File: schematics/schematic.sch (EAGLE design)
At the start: 47 parts, among them IC1 74HC365, T1 BC547, X5 PN61729-S

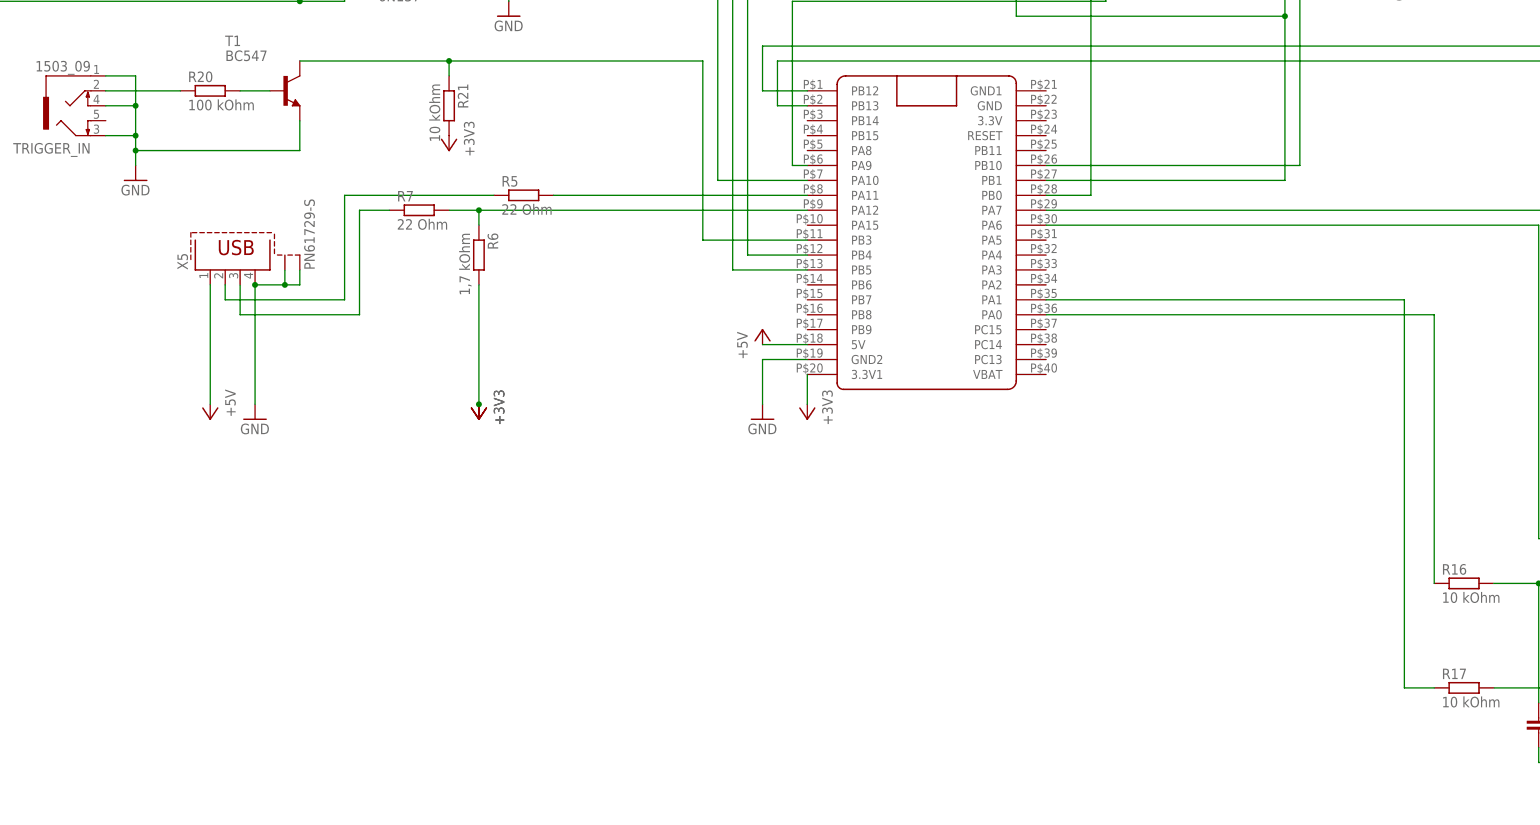
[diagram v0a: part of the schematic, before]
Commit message: added eeprom chip to schematic
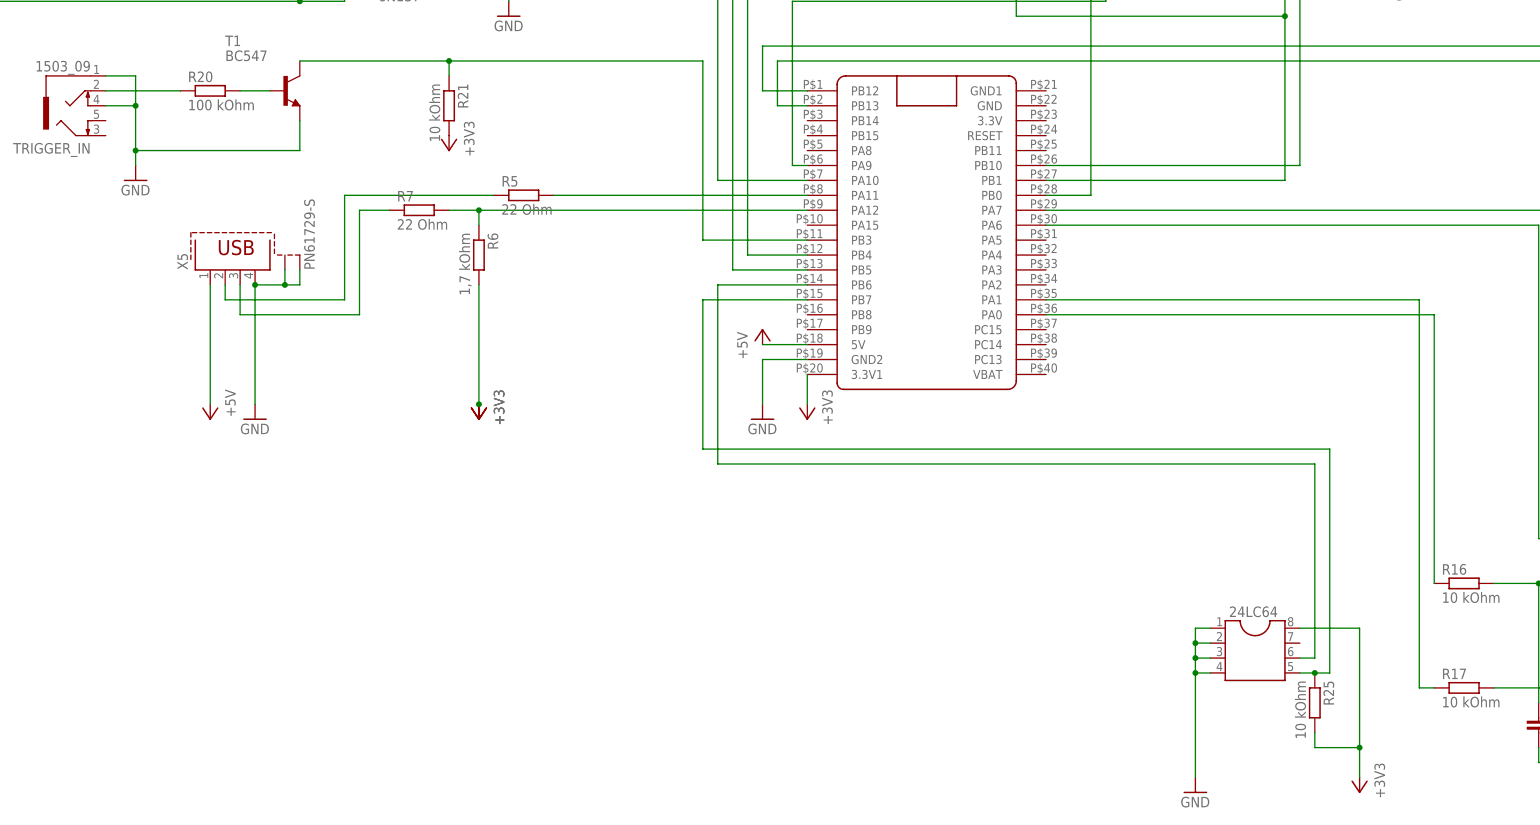
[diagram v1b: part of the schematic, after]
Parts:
- added 24LC64: (no value), ic-package:DIL8
- added R25: 10 kOhm, rcl:R-EU_0207/10
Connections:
- new net PB6: 24LC64.6, U$1.PB6
- new net PB7: 24LC64.5, R25.1, U$1.PB7
- net +3V3: now also 24LC64.8, R25.2
- net GND: now also 24LC64.1, 24LC64.2, 24LC64.3, 24LC64.4; no longer TRIGGER_IN.3
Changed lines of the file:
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@@
 <part name="GND10" library="supply1" library_urn="urn:adsk.eagle:library:371" deviceset="GND" device=""/>
 <part name="R23" library="rcl" library_urn="urn:adsk.eagle:library:334" deviceset="R-EU_" device="0207/10" package3d_urn="urn:adsk.eagle:package:23491/2" value="1 kOhm"/>
+<part name="24LC64" library="ic-package" library_urn="urn:adsk.eagle:library:239" deviceset="DIL8" device="" package3d_urn="urn:adsk.eagle:package:29519/2"/>
+<part name="GND11" library="supply1" library_urn="urn:adsk.eagle:library:371" deviceset="GND" device=""/>
+<part name="+3V5" library="supply1" library_urn="urn:adsk.eagle:library:371" deviceset="+3V3" device=""/>
+<part name="R25" library="rcl" library_urn="urn:adsk.eagle:library:334" deviceset="R-EU_" device="0207/10" package3d_urn="urn:adsk.eagle:package:23491/2" value="10 kOhm"/>
 </parts>
 <sheets>
@@
 <attribute name="NAME" x="148.8186" y="138.43" size="1.778" layer="95" rot="R270"/>
 <attribute name="VALUE" x="144.018" y="138.43" size="1.778" layer="96" rot="R270"/>
+</instance>
+<instance part="24LC64" gate="G$1" x="119.38" y="-25.4" smashed="yes">
+<attribute name="NAME" x="114.935" y="-20.955" size="1.778" layer="95"/>
+<attribute name="VALUE" x="114.935" y="-34.29" size="1.778" layer="96"/>
+</instance>
+<instance part="GND11" gate="1" x="109.22" y="-50.8" smashed="yes">
+<attribute name="VALUE" x="106.68" y="-53.34" size="1.778" layer="96"/>
+</instance>
+<instance part="+3V5" gate="G$1" x="137.16" y="-50.8" smashed="yes" rot="R180">
+<attribute name="VALUE" x="139.7" y="-45.72" size="1.778" layer="96" rot="R270"/>
+</instance>
+<instance part="R25" gate="G$1" x="129.54" y="-35.56" smashed="yes" rot="R270">
+<attribute name="NAME" x="131.0386" y="-31.75" size="1.778" layer="95" rot="R270"/>
+<attribute name="VALUE" x="126.238" y="-31.75" size="1.778" layer="96" rot="R270"/>
 </instance>
 </instances>
@@
 <wire x1="-71.12" y1="71.12" x2="-71.12" y2="66.04" width="0.1524" layer="91"/>
 <pinref part="TRIGGER_IN" gate="G$1" pin="4"/>
-<wire x1="-71.12" y1="66.04" x2="-71.12" y2="60.96" width="0.1524" layer="91"/>
-<wire x1="-71.12" y1="60.96" x2="-71.12" y2="58.42" width="0.1524" layer="91"/>
+<wire x1="-71.12" y1="66.04" x2="-71.12" y2="58.42" width="0.1524" layer="91"/>
 <wire x1="-71.12" y1="58.42" x2="-71.12" y2="55.88" width="0.1524" layer="91"/>
 <wire x1="-76.2" y1="66.04" x2="-71.12" y2="66.04" width="0.1524" layer="91"/>
 <junction x="-71.12" y="66.04"/>
-<pinref part="TRIGGER_IN" gate="G$1" pin="3"/>
-<wire x1="-76.2" y1="60.96" x2="-71.12" y2="60.96" width="0.1524" layer="91"/>
-<junction x="-71.12" y="60.96"/>
 <wire x1="-43.18" y1="58.42" x2="-71.12" y2="58.42" width="0.1524" layer="91"/>
 <junction x="-71.12" y="58.42"/>
@@
 <junction x="139.7" y="147.32"/>
 </segment>
+<segment>
+<pinref part="24LC64" gate="G$1" pin="4"/>
+<pinref part="GND11" gate="1" pin="GND"/>
+<wire x1="111.76" y1="-30.48" x2="109.22" y2="-30.48" width="0.1524" layer="91"/>
+<wire x1="109.22" y1="-30.48" x2="109.22" y2="-48.26" width="0.1524" layer="91"/>
+<pinref part="24LC64" gate="G$1" pin="3"/>
+<wire x1="111.76" y1="-27.94" x2="109.22" y2="-27.94" width="0.1524" layer="91"/>
+<wire x1="109.22" y1="-27.94" x2="109.22" y2="-30.48" width="0.1524" layer="91"/>
+<junction x="109.22" y="-30.48"/>
+<pinref part="24LC64" gate="G$1" pin="2"/>
+<wire x1="111.76" y1="-25.4" x2="109.22" y2="-25.4" width="0.1524" layer="91"/>
+<wire x1="109.22" y1="-25.4" x2="109.22" y2="-27.94" width="0.1524" layer="91"/>
+<junction x="109.22" y="-27.94"/>
+<pinref part="24LC64" gate="G$1" pin="1"/>
+<wire x1="111.76" y1="-22.86" x2="109.22" y2="-22.86" width="0.1524" layer="91"/>
+<wire x1="109.22" y1="-22.86" x2="109.22" y2="-25.4" width="0.1524" layer="91"/>
+<junction x="109.22" y="-25.4"/>
+</segment>
 </net>
 <net name="PB12" class="0">
@@
 <pinref part="+3V4" gate="G$1" pin="+3V3"/>
 </segment>
+<segment>
+<pinref part="24LC64" gate="G$1" pin="8"/>
+<pinref part="+3V5" gate="G$1" pin="+3V3"/>
+<wire x1="127" y1="-22.86" x2="137.16" y2="-22.86" width="0.1524" layer="91"/>
+<wire x1="137.16" y1="-22.86" x2="137.16" y2="-43.18" width="0.1524" layer="91"/>
+<pinref part="R25" gate="G$1" pin="2"/>
+<wire x1="137.16" y1="-43.18" x2="137.16" y2="-48.26" width="0.1524" layer="91"/>
+<wire x1="129.54" y1="-40.64" x2="129.54" y2="-43.18" width="0.1524" layer="91"/>
+<wire x1="129.54" y1="-43.18" x2="137.16" y2="-43.18" width="0.1524" layer="91"/>
+<junction x="137.16" y="-43.18"/>
+</segment>
 </net>
 <net name="PA2" class="0">
@@
 <segment>
 <pinref part="R17" gate="G$1" pin="1"/>
-<wire x1="149.86" y1="-33.02" x2="144.78" y2="-33.02" width="0.1524" layer="91"/>
+<wire x1="149.86" y1="-33.02" x2="147.32" y2="-33.02" width="0.1524" layer="91"/>
 <pinref part="U$1" gate="G$1" pin="PA1"/>
-<wire x1="144.78" y1="-33.02" x2="144.78" y2="33.02" width="0.1524" layer="91"/>
-<wire x1="144.78" y1="33.02" x2="83.82" y2="33.02" width="0.1524" layer="91"/>
+<wire x1="147.32" y1="-33.02" x2="147.32" y2="33.02" width="0.1524" layer="91"/>
+<wire x1="147.32" y1="33.02" x2="83.82" y2="33.02" width="0.1524" layer="91"/>
 </segment>
 </net>
@@
 </segment>
 </net>
+<net name="PB6" class="0">
+<segment>
+<pinref part="U$1" gate="G$1" pin="PB6"/>
+<wire x1="43.18" y1="35.56" x2="27.94" y2="35.56" width="0.1524" layer="91"/>
+<wire x1="27.94" y1="35.56" x2="27.94" y2="5.08" width="0.1524" layer="91"/>
+<wire x1="27.94" y1="5.08" x2="129.54" y2="5.08" width="0.1524" layer="91"/>
+<pinref part="24LC64" gate="G$1" pin="6"/>
+<wire x1="129.54" y1="5.08" x2="129.54" y2="-27.94" width="0.1524" layer="91"/>
+<wire x1="129.54" y1="-27.94" x2="127" y2="-27.94" width="0.1524" layer="91"/>
+</segment>
+</net>
+<net name="PB7" class="0">
+<segment>
+<pinref part="24LC64" gate="G$1" pin="5"/>
+<wire x1="127" y1="-30.48" x2="129.54" y2="-30.48" width="0.1524" layer="91"/>
+<wire x1="129.54" y1="-30.48" x2="132.08" y2="-30.48" width="0.1524" layer="91"/>
+<wire x1="132.08" y1="-30.48" x2="132.08" y2="7.62" width="0.1524" layer="91"/>
+<wire x1="132.08" y1="7.62" x2="25.4" y2="7.62" width="0.1524" layer="91"/>
+<wire x1="25.4" y1="7.62" x2="25.4" y2="33.02" width="0.1524" layer="91"/>
+<pinref part="U$1" gate="G$1" pin="PB7"/>
+<wire x1="25.4" y1="33.02" x2="43.18" y2="33.02" width="0.1524" layer="91"/>
+<pinref part="R25" gate="G$1" pin="1"/>
+<junction x="129.54" y="-30.48"/>
+</segment>
+</net>

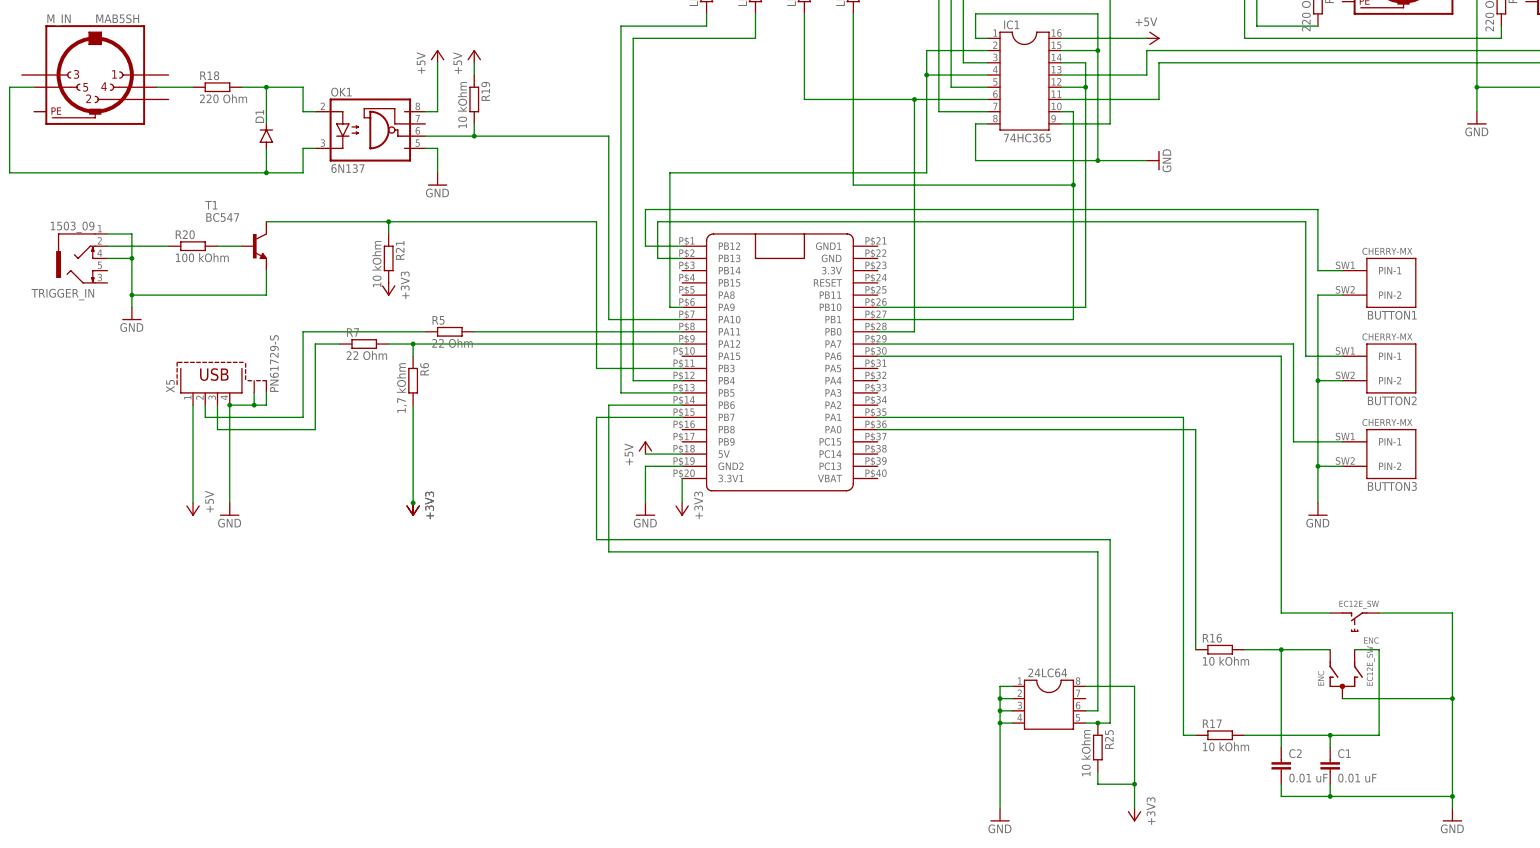
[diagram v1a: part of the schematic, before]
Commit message: added lcd8x2 display
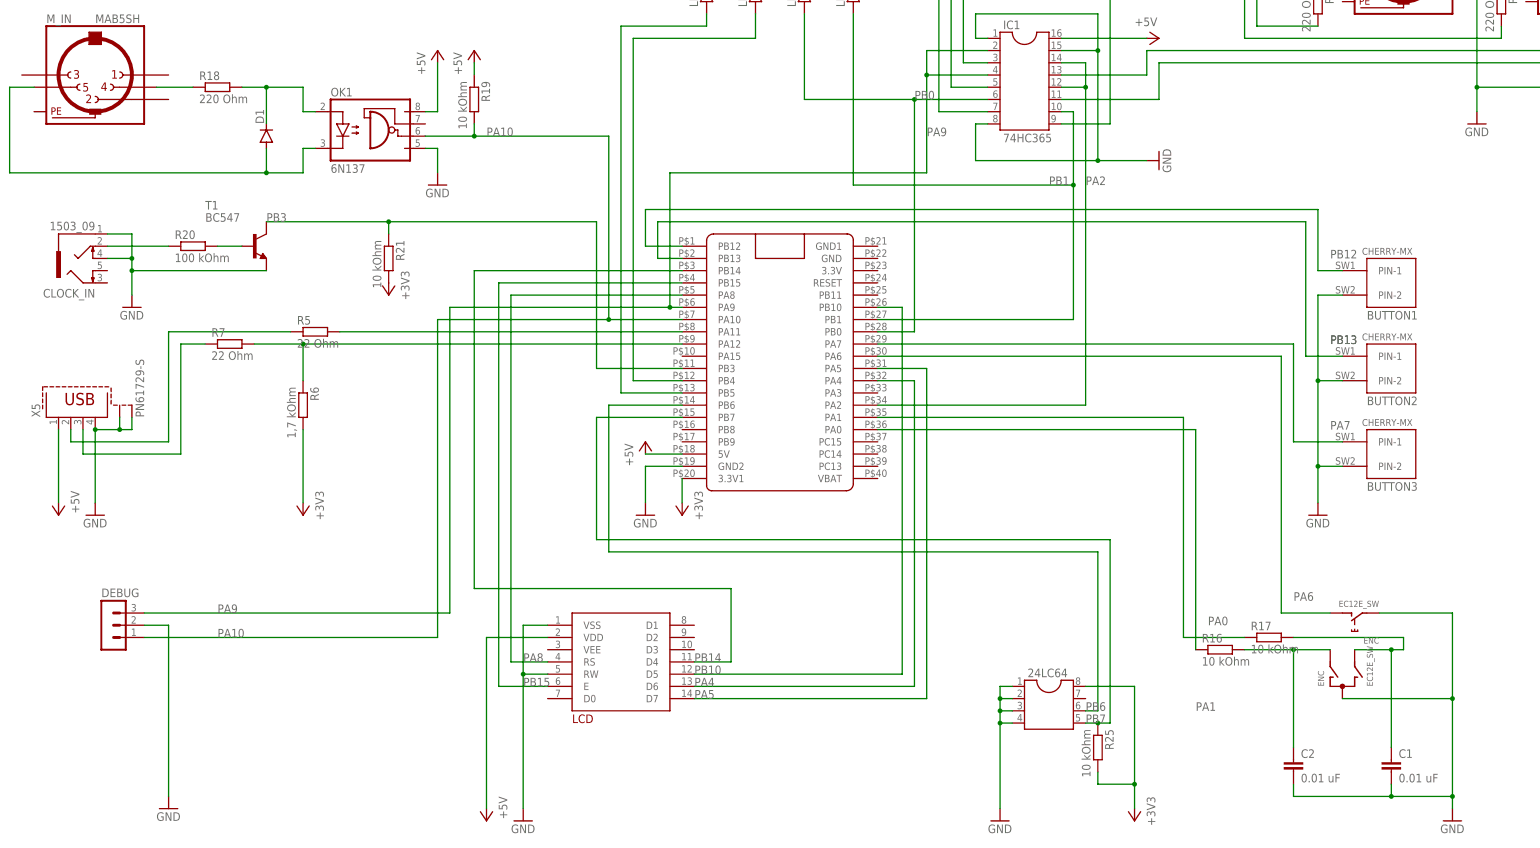
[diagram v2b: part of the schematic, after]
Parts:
- added DEBUG: (no value), con-lstb:MA03-1
- added LCD: LCD-MODUL2X8, lcd082dip:LCD-MODUL2X8
- renumbered TRIGGER_IN to CLOCK_IN
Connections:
- net N$22 renamed PA6
- net N$27 renamed PB3
- new net PA4: LCD.D6, U$1.PA4
- new net PA5: LCD.D7, U$1.PA5
- new net PA8: LCD.RS, U$1.PA8
- new net PA9: DEBUG.3, IC1.2, IC1.4, U$1.PA9
- new net PB14: LCD.D4, U$1.PB14
- new net PB15: LCD.E, U$1.PB15
- net +5V: now also LCD.VDD
- net GND: now also DEBUG.2, LCD.RW, LCD.VSS
- net PA10: now also DEBUG.1
- net PA2: now also IC1.12, IC1.14, U$1.PA2; no longer IC1.2, IC1.4, U$1.PA9
- net PB10: now also LCD.D5; no longer IC1.12, IC1.14
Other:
- moved on the sheet: C1, C2, R17, R5, R6, R7, X5
